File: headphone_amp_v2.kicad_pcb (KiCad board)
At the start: 2 copper layers, 88.9 x 73.7 mm, 75 parts, among them J1 USB_OTG, J2 HID_JMP, J3 AudioJack3_Ground, U1 PCM2707PJTG4, U2 PCM1794A, U3 TPS60501DGS, U4 OPA2134PA, U5 OPA2134PA, U6 LM2662M, Y1 12Mhz

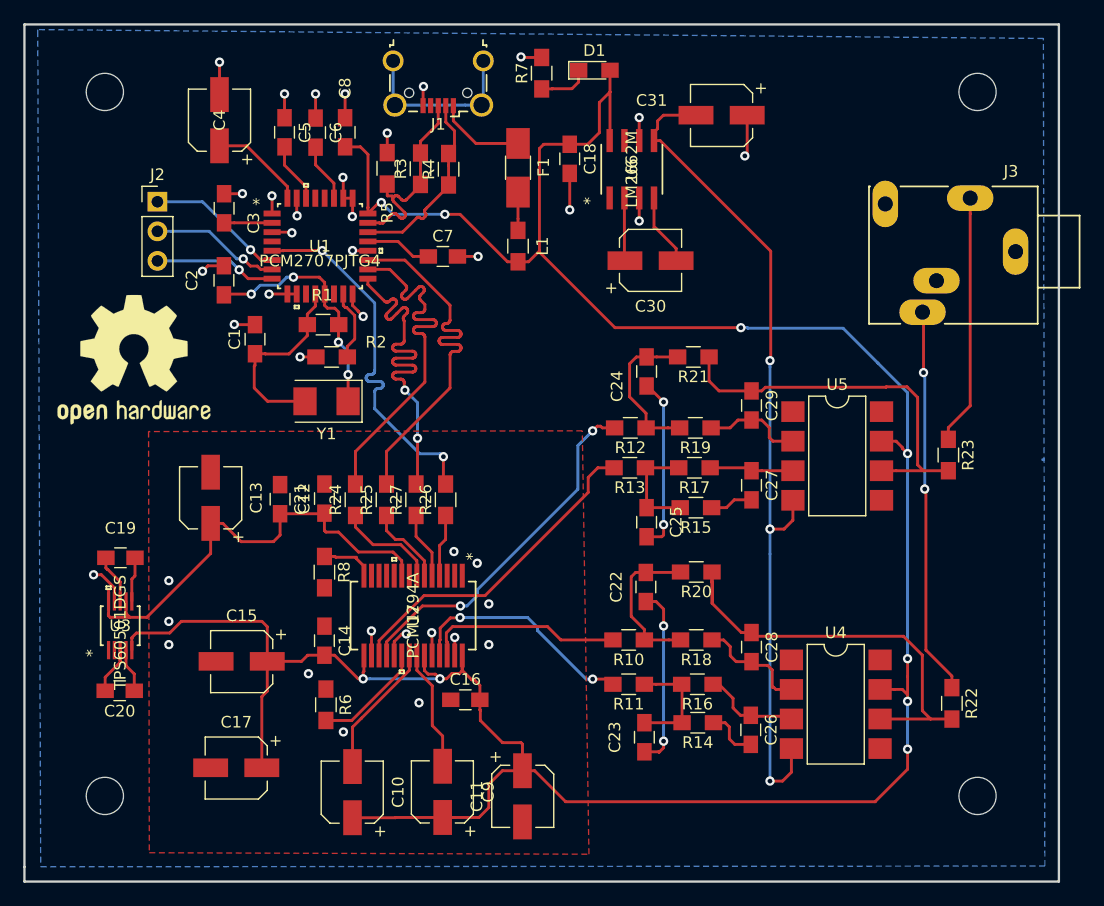
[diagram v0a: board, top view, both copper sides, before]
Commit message: added several testpoints and moved some silkscreen component names for visibility
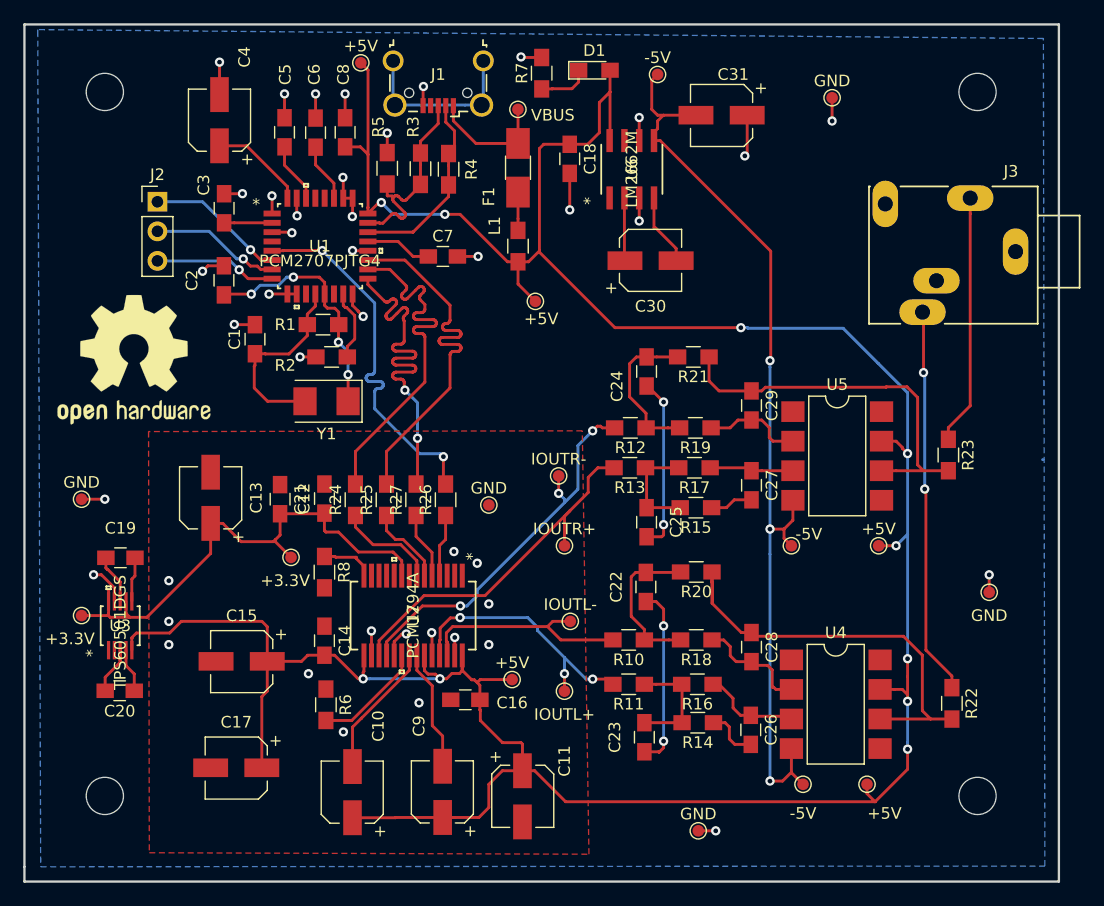
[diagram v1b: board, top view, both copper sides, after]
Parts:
- added +3.3V: TestPoint_Pad_D1.0mm, TestPoint:TestPoint_Pad_D1.0mm, F.Cu at (44.5, 58.5)
- added +3.3V: TestPoint_Pad_D1.0mm, TestPoint:TestPoint_Pad_D1.0mm, F.Cu at (26.5, 63.5)
- added +5V: TestPoint_Pad_D1.0mm, TestPoint:TestPoint_Pad_D1.0mm, F.Cu at (50.5, 16.0)
- added +5V: TestPoint_Pad_D1.0mm, TestPoint:TestPoint_Pad_D1.0mm, F.Cu at (63.5, 69.0)
- added +5V: TestPoint_Pad_D1.0mm, TestPoint:TestPoint_Pad_D1.0mm, F.Cu at (94.0, 78.0)
- added +5V: TestPoint_Pad_D1.0mm, TestPoint:TestPoint_Pad_D1.0mm, F.Cu at (65.5, 36.5)
- added +5V: TestPoint_Pad_D1.0mm, TestPoint:TestPoint_Pad_D1.0mm, F.Cu at (95.0, 57.5)
- added -5V: TestPoint_Pad_D1.0mm, TestPoint:TestPoint_Pad_D1.0mm, F.Cu at (76.0, 17.0)
- added -5V: TestPoint_Pad_D1.0mm, TestPoint:TestPoint_Pad_D1.0mm, F.Cu at (87.5, 57.5)
- added -5V: TestPoint_Pad_D1.0mm, TestPoint:TestPoint_Pad_D1.0mm, F.Cu at (88.5, 78.0)
- added GND: TestPoint_Pad_D1.0mm, TestPoint:TestPoint_Pad_D1.0mm, F.Cu at (91.0, 19.0)
- added GND: TestPoint_Pad_D1.0mm, TestPoint:TestPoint_Pad_D1.0mm, F.Cu at (26.5, 53.5)
- added GND: TestPoint_Pad_D1.0mm, TestPoint:TestPoint_Pad_D1.0mm, F.Cu at (79.5, 82.0)
- added GND: TestPoint_Pad_D1.0mm, TestPoint:TestPoint_Pad_D1.0mm, F.Cu at (104.5, 61.5)
- added GND: TestPoint_Pad_D1.0mm, TestPoint:TestPoint_Pad_D1.0mm, F.Cu at (61.5, 54.0)
- added IOUTL+: TestPoint_Pad_D1.0mm, TestPoint:TestPoint_Pad_D1.0mm, F.Cu at (68.0, 70.0)
- added IOUTL-: TestPoint_Pad_D1.0mm, TestPoint:TestPoint_Pad_D1.0mm, F.Cu at (68.5, 64.0)
- added IOUTR+: TestPoint_Pad_D1.0mm, TestPoint:TestPoint_Pad_D1.0mm, F.Cu at (68.0, 57.5)
- added IOUTR-: TestPoint_Pad_D1.0mm, TestPoint:TestPoint_Pad_D1.0mm, F.Cu at (67.5, 51.5)
- added VBUS: TestPoint_Pad_D1.0mm, TestPoint:TestPoint_Pad_D1.0mm, F.Cu at (64.0, 20.0)
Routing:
- net 5V: track 241.1 -> 261.0 mm, vias 9 -> 10
- net -5V: track 73.0 -> 80.6 mm
- net GND: track 59.9 -> 66.9 mm, vias 39 -> 43
- net 3.3V: track 40.5 -> 44.9 mm
- net IOUTR+: track 28.4 -> 31.6 mm
- net Net-(F1-Pad1): track 7.67 -> 10.6 mm
- net IOUTL+: track 20.2 -> 23.1 mm, vias 2 -> 3
- net IOUTR-: track 31.0 -> 33.5 mm, vias 2 -> 3
- net IOUTL-: track 18.2 -> 20.3 mm

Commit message: length matched the signal traces
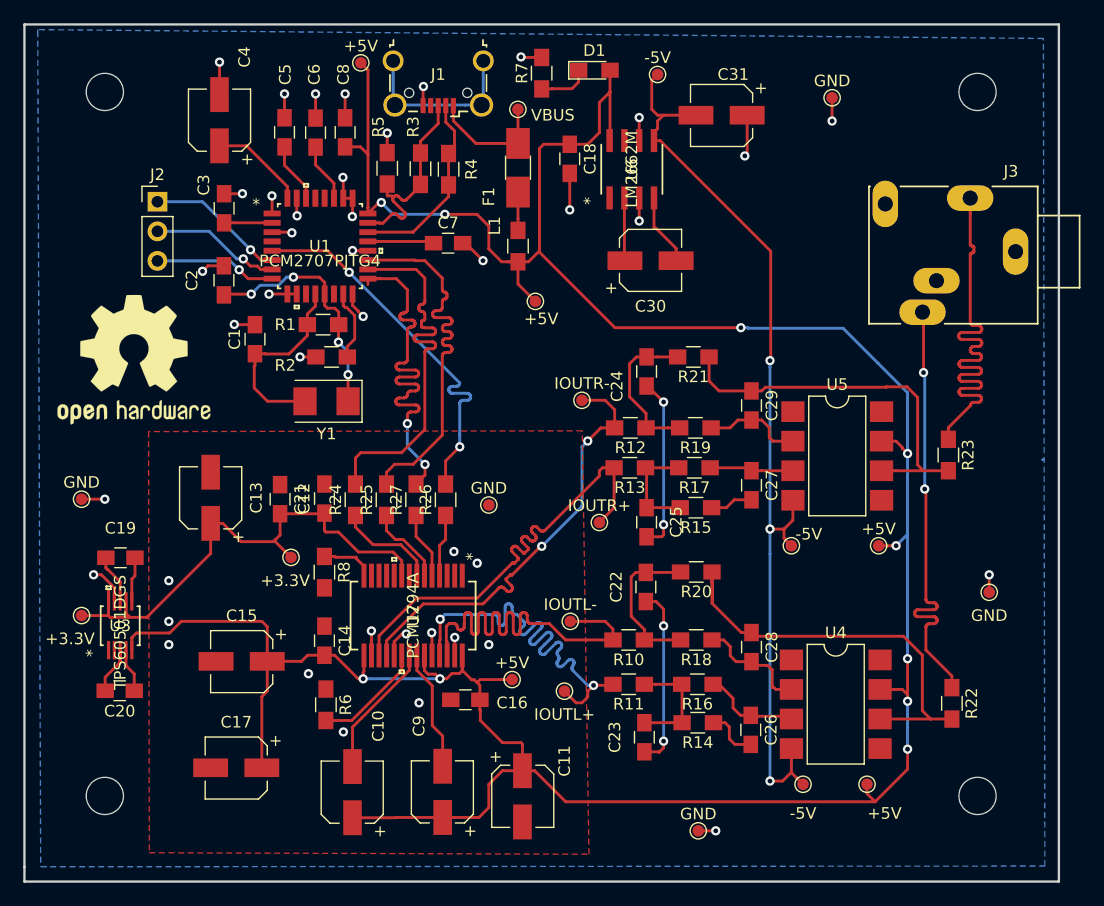
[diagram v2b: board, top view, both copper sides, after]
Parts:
- moved IOUTR- 6.80 mm to (69.5, 45.0)
- moved IOUTR+ 3.61 mm to (71.0, 55.5)
- moved C7 1.22 mm to (58.0, 31.5)
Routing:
- net IOUTL-: track 20.3 -> 37.9 mm
- net OUTR: track 21.5 -> 38.3 mm
- net IOUTL+: track 23.1 -> 39.2 mm, vias 3 -> 2
- net IOUTR+: track 31.6 -> 38.3 mm
- net OUTL: track 33.3 -> 38.1 mm
- net IOUTR-: track 33.5 -> 37.8 mm, vias 3 -> 2
- net DATA_P: track 32.0 -> 34.8 mm
- net 5V: track 261.0 -> 263.1 mm
- net DATA_N: track 32.0 -> 33.6 mm
- net CLK_N: track 32.2 -> 33.2 mm
- net GND: track 66.9 -> 67.5 mm, vias 43 -> 42
